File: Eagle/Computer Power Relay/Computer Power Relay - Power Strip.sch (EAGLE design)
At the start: 7 parts, among them K1 RELAY-3V3DC-110VAC012, K3 RELAY-110VACFLAT-PINS-V2

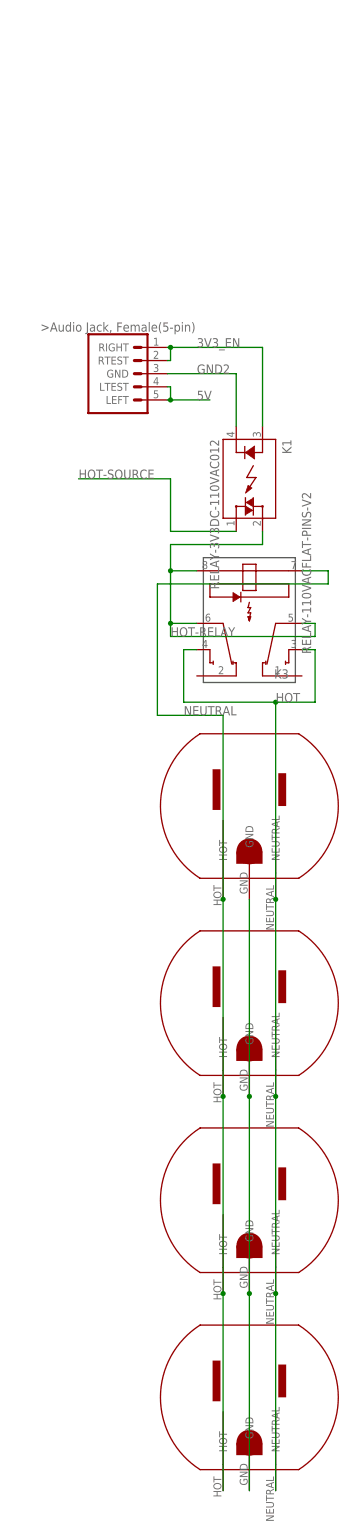
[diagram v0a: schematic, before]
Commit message: Beginning Merge of Boards (Relay)
I'm beginning to merge the Controller and Power Strip boards into one so that I can print it for cheaper.
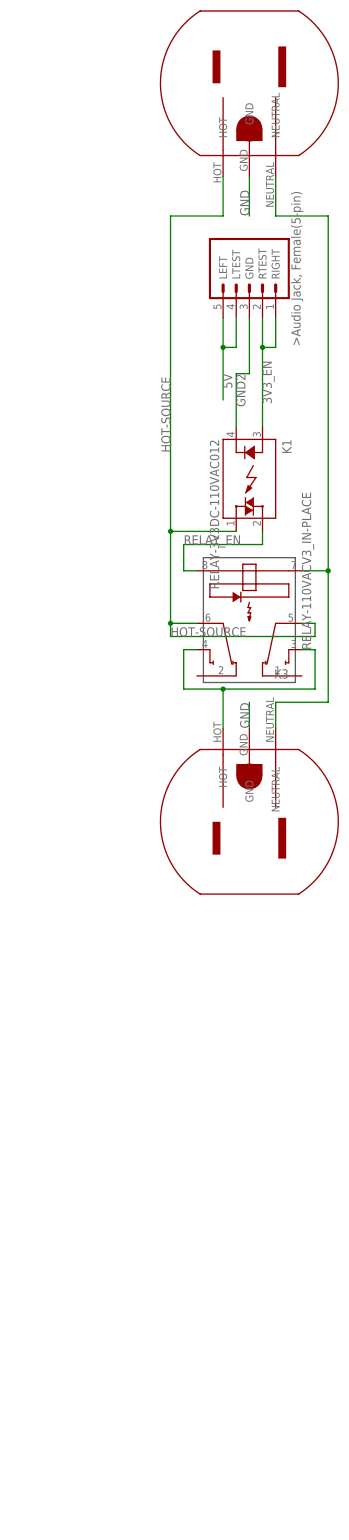
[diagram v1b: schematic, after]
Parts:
- removed U$4, U$5, U$6: MAINS-POWER-OUTLET, KVM Keyboard:MAINS-POWER-OUTLET
- added U$2: MAINS-POWER-OUTLET3-PIN, Inventory:MAINS-POWER-OUTLET3-PIN
- K3: value RELAY-110VACFLAT-PINS-V2 -> RELAY-110VACV3_IN-PLACE; device Inventory:RELAY-110VACFLAT-PINS-V2 -> Inventory:RELAY-110VACV3_IN-PLACE
- U$3: value MAINS-POWER-OUTLET -> MAINS-POWER-OUTLET3-PIN; device KVM Keyboard:MAINS-POWER-OUTLET -> Inventory:MAINS-POWER-OUTLET3-PIN
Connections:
- removed net HOT: K3.3, K3.4, U$3.NEUTRAL, U$4.NEUTRAL, U$5.NEUTRAL, U$6.NEUTRAL
- removed net HOT-RELAY: K1.2, K3.5, K3.6, K3.8
- removed net N$9: U$3.GND, U$4.GND, U$5.GND, U$6.GND
- removed net NEUTRAL: K3.7, U$3.HOT, U$4.HOT, U$5.HOT, U$6.HOT
- new net GND: U$2.GND, U$3.GND
- new net N$1: K3.3, K3.4, U$2.HOT
- new net N$2: K3.7, U$2.NEUTRAL, U$3.NEUTRAL
- new net RELAY_EN: K1.2, K3.8
- net HOT-SOURCE: now also K3.5, K3.6, U$3.HOT
